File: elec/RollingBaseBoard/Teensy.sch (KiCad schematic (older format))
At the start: 13 parts, among them P14 Encoder2, P15 Motor, U3 Teensy3.1

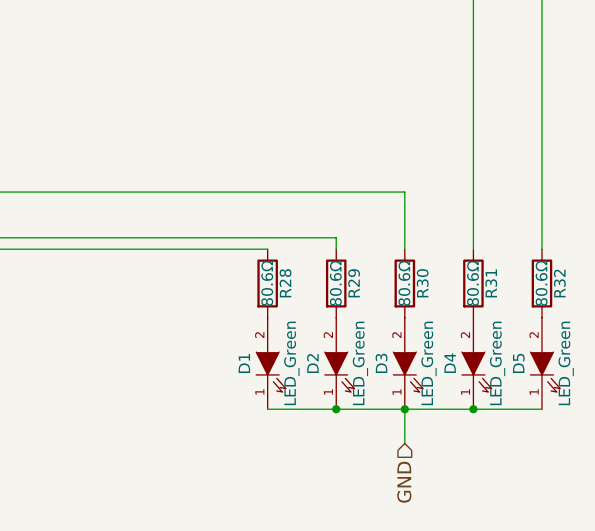
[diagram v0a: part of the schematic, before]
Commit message: Updated the schematics to use the proper footprints.
Also regenerated the net list file.
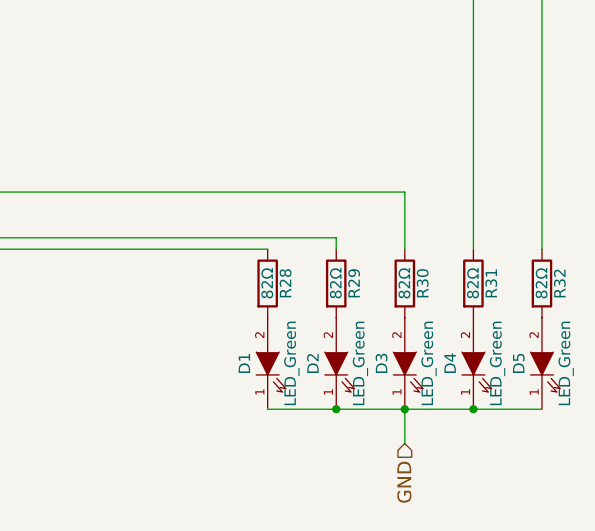
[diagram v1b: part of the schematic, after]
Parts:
- D1, D2, D3, D4, D5: footprint (none) -> Footprints:LED_Green_CMS
- P14: footprint (none) -> Footprints:Conn_01x02
- P15: footprint (none) -> Footprints:Conn_01x03
- R28, R29, R30, R31, R32: value 80.6Ω -> 82Ω; footprint (none) -> Footprints:R_CMS1206
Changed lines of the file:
@@
 F 0 "P14" H 4650 4950 50  0000 C CNN
 F 1 "Encoder2" V 4750 4800 50  0000 C CNN
-F 2 "" H 4650 4800 60  0000 C CNN
+F 2 "Footprints:Conn_01x02" H 4650 4800 60  0001 C CNN
 F 3 "" H 4650 4800 60  0000 C CNN
 	1    4650 4800
@@
 P 7150 4650
 F 0 "R28" V 7230 4650 50  0000 C CNN
-F 1 "80.6Ω" V 7150 4650 50  0000 C CNN
-F 2 "" V 7080 4650 30  0000 C CNN
+F 1 "82Ω" V 7150 4650 50  0000 C CNN
+F 2 "Footprints:R_CMS1206" V 7080 4650 30  0001 C CNN
 F 3 "" H 7150 4650 30  0000 C CNN
 	1    7150 4650
@@
 F 0 "D1" H 7150 5100 50  0000 C CNN
 F 1 "LED_Green" H 7150 4900 50  0000 C CNN
-F 2 "" H 7150 5000 60  0000 C CNN
+F 2 "Footprints:LED_Green_CMS" H 7150 5000 60  0001 C CNN
 F 3 "" H 7150 5000 60  0000 C CNN
 	1    7150 5000
@@
 P 7450 4650
 F 0 "R29" V 7530 4650 50  0000 C CNN
-F 1 "80.6Ω" V 7450 4650 50  0000 C CNN
-F 2 "" V 7380 4650 30  0000 C CNN
+F 1 "82Ω" V 7450 4650 50  0000 C CNN
+F 2 "Footprints:R_CMS1206" V 7380 4650 30  0001 C CNN
 F 3 "" H 7450 4650 30  0000 C CNN
 	1    7450 4650
@@
 P 7750 4650
 F 0 "R30" V 7830 4650 50  0000 C CNN
-F 1 "80.6Ω" V 7750 4650 50  0000 C CNN
-F 2 "" V 7680 4650 30  0000 C CNN
+F 1 "82Ω" V 7750 4650 50  0000 C CNN
+F 2 "Footprints:R_CMS1206" V 7680 4650 30  0001 C CNN
 F 3 "" H 7750 4650 30  0000 C CNN
 	1    7750 4650
@@
 P 8050 4650
 F 0 "R31" V 8130 4650 50  0000 C CNN
-F 1 "80.6Ω" V 8050 4650 50  0000 C CNN
-F 2 "" V 7980 4650 30  0000 C CNN
+F 1 "82Ω" V 8050 4650 50  0000 C CNN
+F 2 "Footprints:R_CMS1206" V 7980 4650 30  0001 C CNN
 F 3 "" H 8050 4650 30  0000 C CNN
 	1    8050 4650
@@
 P 8350 4650
 F 0 "R32" V 8430 4650 50  0000 C CNN
-F 1 "80.6Ω" V 8350 4650 50  0000 C CNN
-F 2 "" V 8280 4650 30  0000 C CNN
+F 1 "82Ω" V 8350 4650 50  0000 C CNN
+F 2 "Footprints:R_CMS1206" V 8280 4650 30  0001 C CNN
 F 3 "" H 8350 4650 30  0000 C CNN
 	1    8350 4650
@@
 F 0 "D2" H 7450 5100 50  0000 C CNN
 F 1 "LED_Green" H 7450 4900 50  0000 C CNN
-F 2 "" H 7450 5000 60  0000 C CNN
+F 2 "Footprints:LED_Green_CMS" H 7450 5000 60  0001 C CNN
 F 3 "" H 7450 5000 60  0000 C CNN
 	1    7450 5000
@@
 F 0 "D3" H 7750 5100 50  0000 C CNN
 F 1 "LED_Green" H 7750 4900 50  0000 C CNN
-F 2 "" H 7750 5000 60  0000 C CNN
+F 2 "Footprints:LED_Green_CMS" H 7750 5000 60  0001 C CNN
 F 3 "" H 7750 5000 60  0000 C CNN
 	1    7750 5000
@@
 F 0 "D4" H 8050 5100 50  0000 C CNN
 F 1 "LED_Green" H 8050 4900 50  0000 C CNN
-F 2 "" H 8050 5000 60  0000 C CNN
+F 2 "Footprints:LED_Green_CMS" H 8050 5000 60  0001 C CNN
 F 3 "" H 8050 5000 60  0000 C CNN
 	1    8050 5000
@@
 F 0 "D5" H 8350 5100 50  0000 C CNN
 F 1 "LED_Green" H 8350 4900 50  0000 C CNN
-F 2 "" H 8350 5000 60  0000 C CNN
+F 2 "Footprints:LED_Green_CMS" H 8350 5000 60  0001 C CNN
 F 3 "" H 8350 5000 60  0000 C CNN
 	1    8350 5000
@@
 F 0 "P15" H 5150 5150 50  0000 C CNN
 F 1 "Motor" V 5250 4950 50  0000 C CNN
-F 2 "" H 5150 4950 60  0000 C CNN
+F 2 "Footprints:Conn_01x03" H 5150 4950 60  0001 C CNN
 F 3 "" H 5150 4950 60  0000 C CNN
 	1    5150 4950
